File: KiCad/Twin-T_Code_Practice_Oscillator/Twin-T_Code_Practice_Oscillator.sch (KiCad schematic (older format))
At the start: 45 parts, among them J1 BATT, J2 DC IN, J3 PITCH, J4 VOLUME, J5 KEY, J6 PHONES, J7 SPKR, Q1 PN2222A, Q2 2N7000, U1 TLV272, U2 LM386

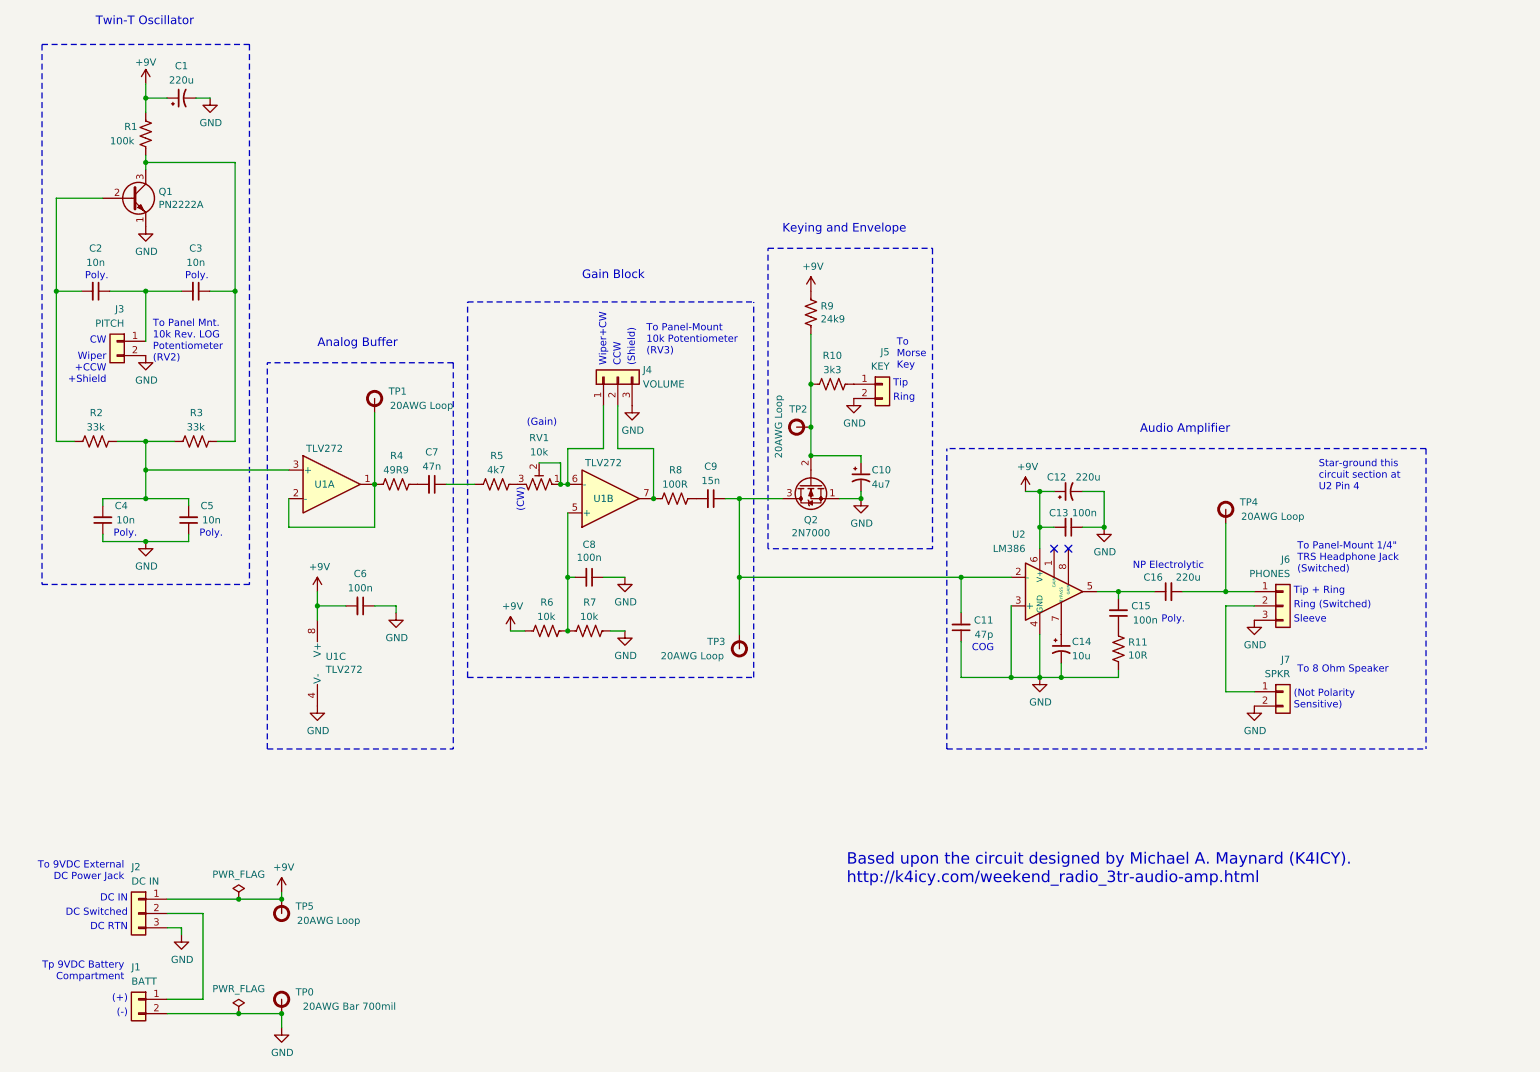
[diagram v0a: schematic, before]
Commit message: Swapped LM386 inputs, tweaked PCB layout, updated BOM
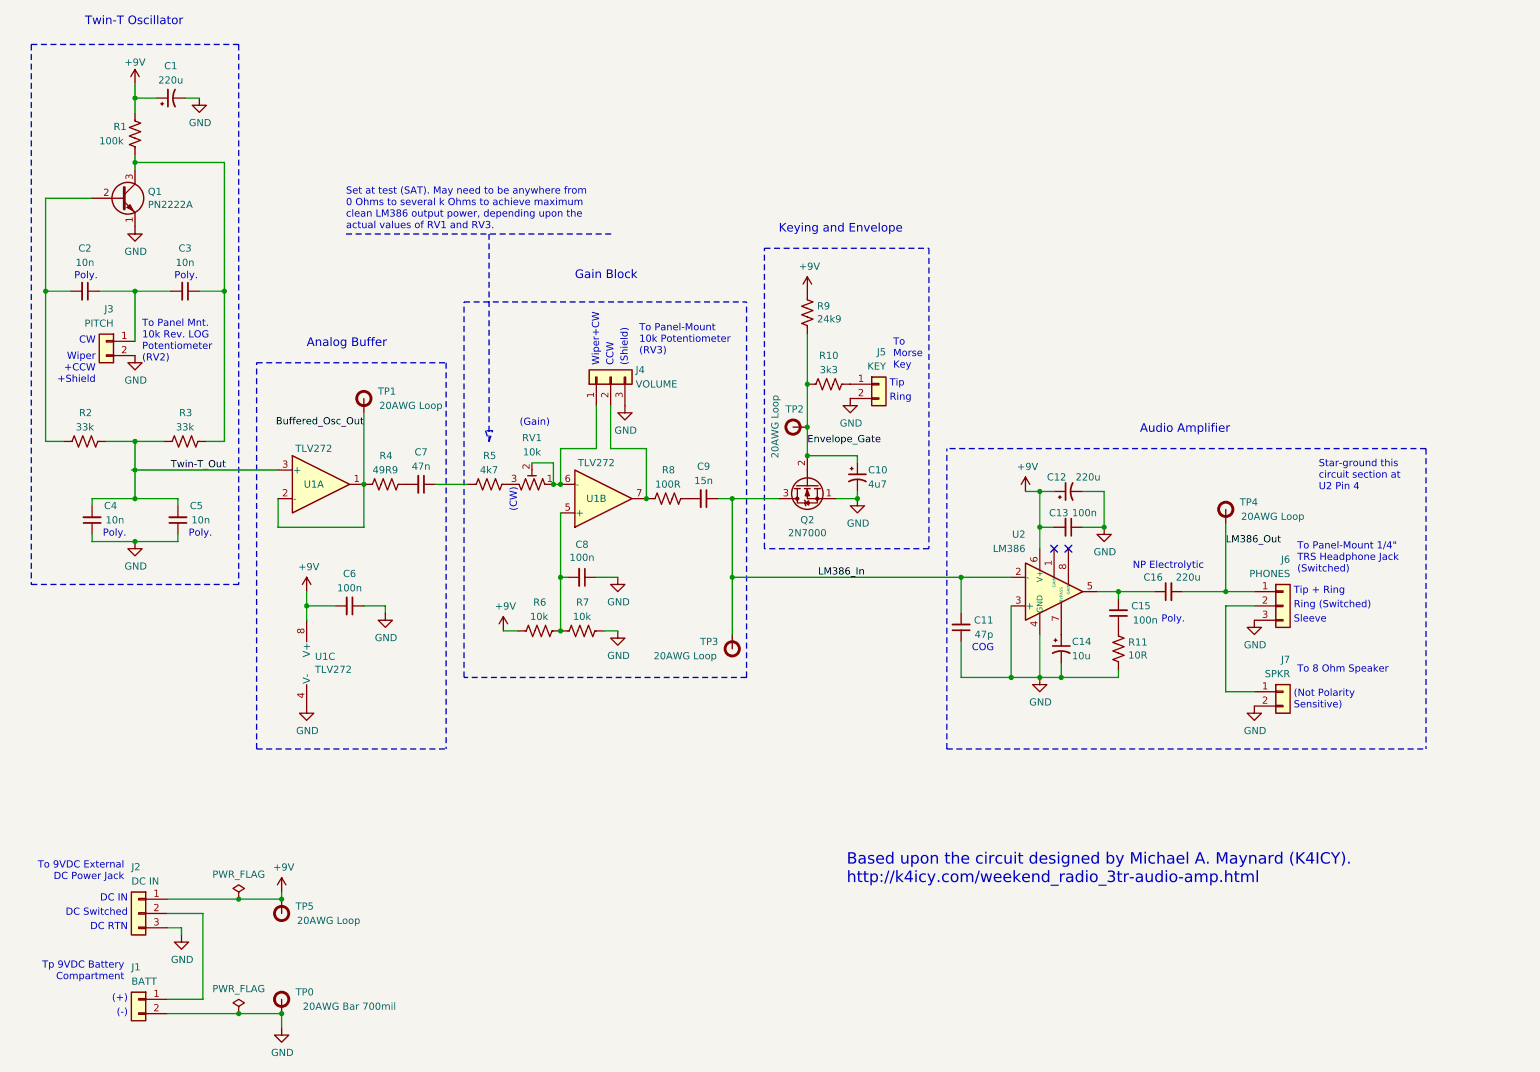
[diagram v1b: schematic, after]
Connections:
- net Envelope_Gate: now reaches C10.1, Q2.2 (G), R10.1, R9.2, TP2.1 (A)
- net Buffered_Osc_Out: now reaches R4.1, TP1.1 (A), U1.1, U1.2 (-)
- net Twin-T_Out: now reaches C4.2, C5.2, R2.2, R3.1, U1.3 (+)
- net LM386_In: now reaches C11.2, C9.1, Q2.3 (D), TP3.1 (A), U2.2 (-)
- net LM386_Out: now reaches C16.2, J6.1 (Pin_1), TP4.1 (A)
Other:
- note added: "Set at test (SAT). May need to be anywhere from\n0 Ohms to several k Ohms to achieve maximum\nclean LM386 output power, depending upon the\nactual values of RV1 and RV3."
- moved on the sheet: C1, C10, C2, C3, C4, C5, C6, C7, C8, C9, J3, J4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

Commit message: Replaced RV1. Cleaned up all docs
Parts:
- RV1: footprint BE_TrimPot:Bourns_3329S_Vertical -> BE_TrimPot:Piher_PT6_Vertical
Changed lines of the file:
@@
 Sheet 1 1
 Title "Twin-T Morse Code Practice Oscillator"
-Date "2020-09-01"
+Date "2020-09-02"
 Rev "A"
 Comp ""
@@
 F 0 "RV1" V 4425 3900 50  0000 C CNN
 F 1 "10k" V 4325 3900 50  0000 C CNN
-F 2 "BE_TrimPot:Bourns_3329S_Vertical" H 4100 3900 50  0001 C CNN
-F 3 "https://www.bourns.com/pdfs/3329.pdf" H 4100 3900 50  0001 C CNN
+F 2 "BE_TrimPot:Piher_PT6_Vertical" H 4100 3900 50  0001 C CNN
+F 3 "https://www.mouser.com/datasheet/2/18/11-PT6v03-1499160.pdf" H 4100 3900 50  0001 C CNN
 	1    4100 3900
 	0    1    -1   0
